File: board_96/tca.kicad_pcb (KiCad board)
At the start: 2 copper layers, 143 x 74 mm, 170 parts, among them IC1 ATMEGA328-A, P1 CONN_2, P2 CONN_3X2, Q1 BSS138, U1 SD_CARD, U10 TLC5941, U11 TLC5941, U12 TLC5941, U13 TLC5941, U14 TLC5941, U15 TLC5941, U2 LD1117S50, U3 LD1117S33, U4 TLC5941, U5 TLC5941, U6 TLC5941, U7 TLC5941, U8 TLC5941, U9 TLC5941, Y1 RESONATEUR

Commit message: Deleted unnecessary files and updated Tlc library.
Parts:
- P1: footprint PIN_ARRAY_2X1 -> PIN_ARRAY_2X1_3960um
- moved C3 3.70 mm to (75.0, 165.7)
- moved P1 2.91 mm to (71.9, 164.7)
- moved 1PIN1 0.50 mm to (207.0, 158.5)
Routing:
- net (no net): track 2096.7 -> 0.00 mm, vias 140 -> 0
- net /tlcs_1-6/VCC: track 80.8 -> 665.3 mm, vias 0 -> 11
- net /tlcs_1-6/SCLK: track 29.4 -> 520.6 mm, vias 12 -> 24
- net /tlcs_1-6/XLAT: track 32.1 -> 521.2 mm, vias 12 -> 19
- net /tlcs_1-6/MODE: track 53.2 -> 528.1 mm, vias 12 -> 29
- net /tlcs_1-6/GSCLK: track 23.5 -> 487.4 mm, vias 12 -> 26
- net /tlcs_1-6/BLANK: track 30.5 -> 405.6 mm, vias 12 -> 20
- net GND: track 400.8 -> 676.8 mm, vias 12 -> 17
- net /tlcs_1-6/SIN: track 2.77 -> 134.9 mm, vias 1 -> 2
- net /MISO: track 0.00 -> 70.2 mm
- net N-00000267: track 4.41 -> 70.7 mm, vias 2 -> 6
- net N-00000183: track 4.41 -> 61.6 mm, vias 2 -> 6
- net N-00000184: track 4.41 -> 60.3 mm, vias 2 -> 6
- net /tlcs_7-12/SIN: track 4.41 -> 56.1 mm, vias 2 -> 1
- net /VSD: track 0.00 -> 47.4 mm, vias 0 -> 2
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- added copper zone on F.Cu, net GND
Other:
- board text added: "TCA96 Rice U Tabor Lab Evan Olson Sebastian Castillo"

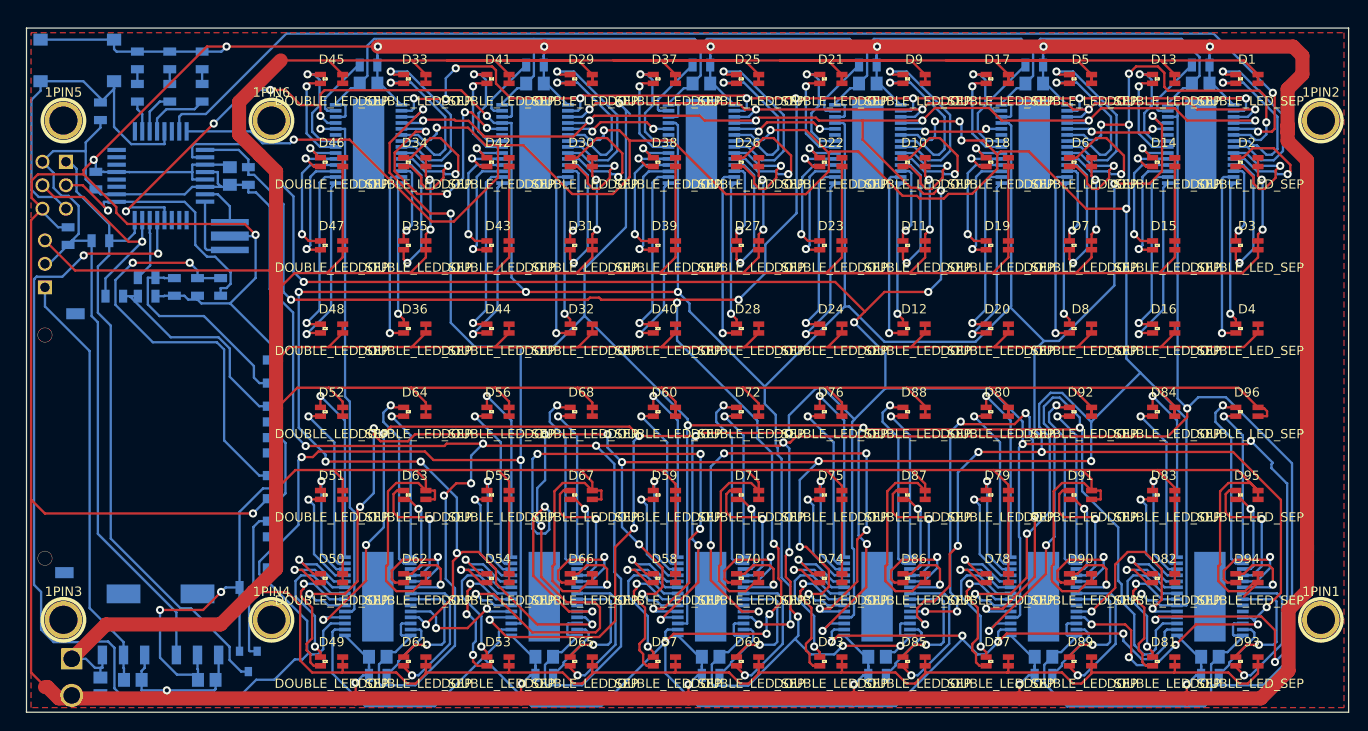
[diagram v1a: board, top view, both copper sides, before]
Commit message: Made board_24_v2 which uses PCB-mounted LED sockets and updated various issues on board_96 as well. These PCBs were ordered around 7/1/14.
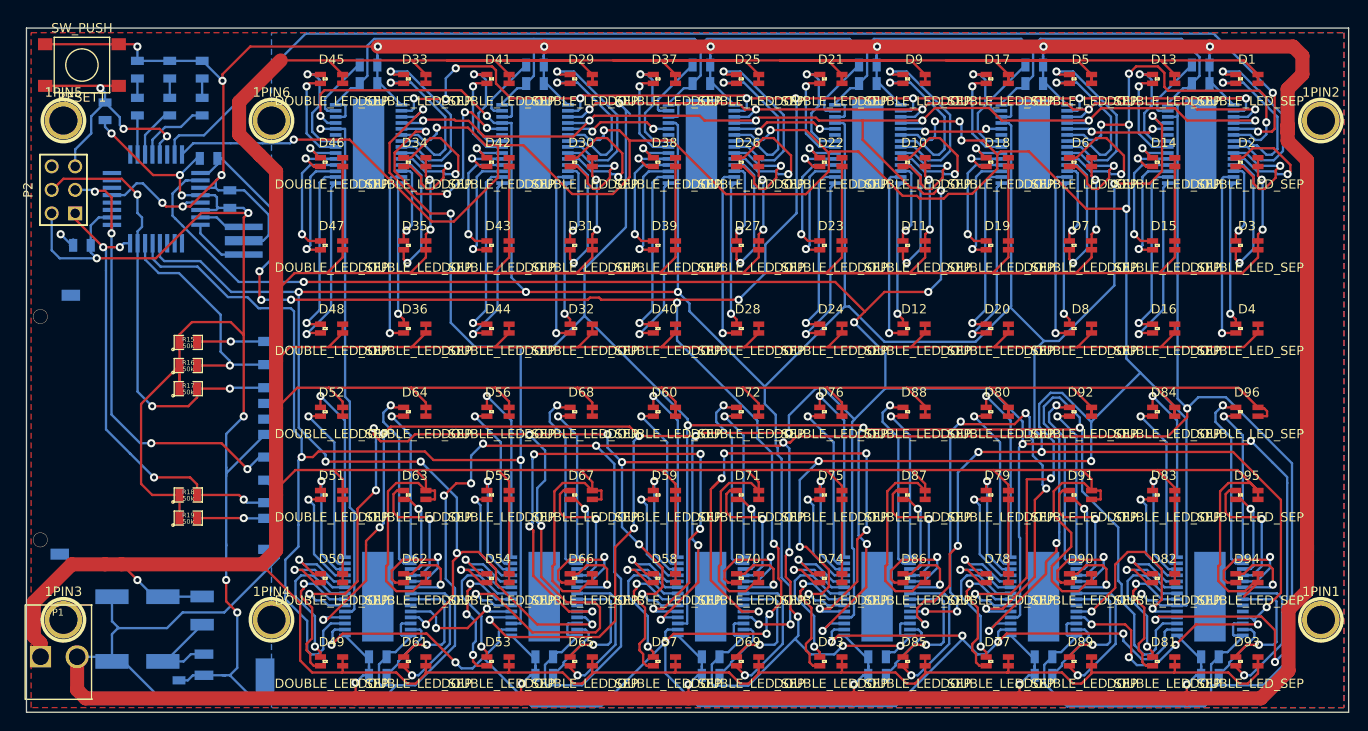
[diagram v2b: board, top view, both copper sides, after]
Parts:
- removed C18: 0.1 uF, c_0805_FIXED
- removed JP1: JUMPER3, PIN_ARRAY_3X1
- removed Q1: BSS138, SOT23
- removed R20, R21, R22: 2.2K, SM0805
- removed U15: TLC5941, TLC5940_FIXED
- added L1: 10uH, SM1210, B.Cu at (86.0, 157.5)
- C1, C10, C11, C12, C13, C14, C15, C16, C17, C2, C5, C7: footprint c_0805_FIXED -> SM0805
- C3, C4: value 100nF -> 47uF; footprint c_0805_FIXED -> c_elec_6.3x5.3
- C6: value 10uF -> 0.1 uF; footprint c_0805_FIXED -> SM0805
- P1, P2, RESET1: moved to F.Cu
- R1: value 10k -> 10K
- R10, R7: value 10K -> 2.2K
- R15, R16, R17, R18, R19: value 2.2K -> 50k; moved to F.Cu
- R2: value 20k -> 10K
- R3, R4, R6, R8: value 10k -> 2.2K
- R5, R9: value 20k -> 2.2K
- U2: value LD1117S50 -> LD1117S33
- U3: value LD1117S33 -> TLC5941; footprint SOT223 -> TLC5940_FIXED
- moved C6 125.4 mm to (194.0, 100.5), turned to 0 degrees
- moved U3 120.3 mm to (194.0, 107.0), turned to 270 degrees
- moved R3 117.5 mm to (194.0, 98.5), turned to 180 degrees
- moved C11 110.1 mm to (104.0, 100.5)
- moved R4 102.6 mm to (176.0, 98.5)
- moved C16 95.8 mm to (177.0, 162.5)
- moved C17 95.8 mm to (195.0, 162.5)
- moved C8 88.1 mm to (158.0, 100.5), turned to 0 degrees
- moved R14 85.9 mm to (195.0, 164.5), turned to 0 degrees
- moved R11 84.6 mm to (141.0, 164.5), turned to 0 degrees
- moved C10 82.9 mm to (122.0, 100.5)
- moved R5 81.9 mm to (158.0, 98.5), turned to 180 degrees
- moved C14 81.6 mm to (141.0, 162.5)
- moved C1 71.8 mm to (89.0, 113.0), turned to 270 degrees
- moved C13 71.2 mm to (123.0, 162.5)
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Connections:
- C4 pad 1: /tlcs_1-6/VCC -> N-0000020
- C5 pad 1: N-0000037 -> /tlcs_1-6/VCC
- C6 pad 1: /VSD -> /tlcs_1-6/VCC
- D1 pad 2: N-00000136 -> N-00000131
- D1 pad 3: N-00000135 -> N-00000130
- D10 pad 2: N-00000120 -> N-00000115
- D10 pad 3: N-00000119 -> N-00000114
- D11 pad 2: N-00000124 -> N-00000119
- D11 pad 3: N-00000122 -> N-00000117
- D12 pad 2: N-00000115 -> N-00000110
- D12 pad 3: N-00000126 -> N-00000121
- D13 pad 2: N-00000143 -> N-00000138
- D13 pad 3: N-00000141 -> N-00000136
- D14 pad 2: N-00000139 -> N-00000134
- D14 pad 3: N-00000150 -> N-00000145
- D15 pad 2: N-00000149 -> N-00000144
- D15 pad 3: N-00000148 -> N-00000143
- D16 pad 2: N-00000147 -> N-00000142
- D16 pad 3: N-00000146 -> N-00000141
- D17 pad 2: N-00000109 -> N-00000104
- D17 pad 3: N-00000107 -> N-00000102
- D18 pad 2: N-00000105 -> N-00000100
- D18 pad 3: N-00000153 -> N-00000148
- D19 pad 2: N-00000152 -> N-00000147
- D19 pad 3: N-00000151 -> N-00000146
- D2 pad 2: N-00000138 -> N-00000133
- D2 pad 3: N-00000137 -> N-00000132
- D20 pad 2: N-00000114 -> N-00000109
- D20 pad 3: N-00000113 -> N-00000108
- D21 pad 2: N-00000125 -> N-00000120
- D21 pad 3: N-00000123 -> N-00000118
- D22 pad 2: N-00000121 -> N-00000116
- D22 pad 3: N-00000133 -> N-00000128
- D23 pad 2: N-00000132 -> N-00000127
- D23 pad 3: N-00000130 -> N-00000125
- D24 pad 2: N-00000129 -> N-00000124
- D24 pad 3: N-00000128 -> N-00000123
- D25 pad 2: N-0000079 -> N-0000073
- D25 pad 3: N-0000080 -> N-0000074
- D26 pad 2: N-0000081 -> N-0000075
- D26 pad 3: N-0000082 -> N-0000076
- D27 pad 2: N-0000083 -> N-0000077
- D27 pad 3: N-0000084 -> N-0000078
- D28 pad 2: N-0000078 -> N-0000072
- D28 pad 3: N-0000077 -> N-0000071
- D29 pad 2: N-0000049 -> N-0000044
- D29 pad 3: N-0000050 -> N-0000045
- D3 pad 2: N-00000142 -> N-00000137
- D3 pad 3: N-00000140 -> N-00000135
- D30 pad 2: N-0000047 -> N-0000042
- D30 pad 3: N-0000048 -> N-0000043
- D31 pad 2: N-0000045 -> N-0000040
- D31 pad 3: N-0000046 -> N-0000041
- D32 pad 2: N-0000043 -> N-0000038
- D32 pad 3: N-0000044 -> N-0000039
- D33 pad 2: N-0000067 (its old number) -> N-0000061
- D33 pad 3: N-0000068 -> N-0000062
- D34 pad 2: N-0000065 (its old number) -> N-0000059
- D34 pad 3: N-0000066 (its old number) -> N-0000060
- D35 pad 2: N-0000064 -> N-0000058
- D35 pad 3: N-0000061 -> N-0000055
- D36 pad 2: N-0000062 -> N-0000056
- D36 pad 3: N-0000063 -> N-0000057
- D37 pad 2: N-0000093 -> N-0000087
- D37 pad 3: N-0000094 -> N-0000088
- D38 pad 2: N-0000095 -> N-0000089
- D38 pad 3: N-0000096 -> N-0000090
- D39 pad 2: N-0000097 -> N-0000091
- D39 pad 3: N-0000060 -> N-0000092
- D4 pad 2: N-00000134 -> N-00000129
- D4 pad 3: N-00000144 -> N-00000139
- D40 pad 2: N-0000098 -> N-0000093
- D40 pad 3: N-0000099 -> N-0000094
- D41 pad 2: N-0000059 -> N-0000054
- D41 pad 3: N-0000058 -> N-0000053
- D42 pad 2: N-0000057 -> N-0000052
- D42 pad 3: N-0000056 -> N-0000051
- D43 pad 2: N-0000055 -> N-0000050
- D43 pad 3: N-0000054 -> N-0000049
- D44 pad 2: N-0000053 -> N-0000048
- D44 pad 3: N-0000052 -> N-0000047
- D45 pad 2: N-0000086 -> N-0000080
- D45 pad 3: N-0000085 -> N-0000079
- D46 pad 2: N-0000087 -> N-0000081
- D46 pad 3: N-0000088 -> N-0000082
- D47 pad 2: N-0000089 -> N-0000083
- D47 pad 3: N-0000090 -> N-0000084
- D48 pad 2: N-0000091 -> N-0000085
- D48 pad 3: N-0000092 -> N-0000086
- D49 pad 2: N-00000248 -> N-00000243
- D49 pad 3: N-00000247 -> N-00000242
- D5 pad 2: N-00000103 -> N-0000098
- D5 pad 3: N-00000102 -> N-0000097
- D50 pad 2: N-00000250 -> N-00000245
- D50 pad 3: N-00000249 -> N-00000244
- D51 pad 2: N-00000254 -> N-00000249
- D51 pad 3: N-00000252 -> N-00000247
- D52 pad 2: N-00000258 -> N-00000253
- D52 pad 3: N-00000256 -> N-00000251
- D53 pad 2: N-00000216 -> N-00000211
- D53 pad 3: N-00000215 -> N-00000210
- D54 pad 2: N-00000213 -> N-00000208
- D54 pad 3: N-00000217 -> N-00000212
- D55 pad 2: N-00000221 -> N-00000216
- D55 pad 3: N-00000219 -> N-00000214
- D56 pad 2: N-00000225 -> N-00000220
- D56 pad 3: N-00000223 -> N-00000218
- D57 pad 2: N-00000229 -> N-00000224
- D57 pad 3: N-00000228 -> N-00000223
- D58 pad 2: N-00000231 -> N-00000226
- D58 pad 3: N-00000230 -> N-00000225
- D59 pad 2: N-00000235 -> N-00000230
- D59 pad 3: N-00000233 -> N-00000228
- D6 pad 2: N-00000104 -> N-0000099
- D6 pad 3: N-00000100 -> N-0000095
- D60 pad 2: N-00000239 -> N-00000234
- D60 pad 3: N-00000237 -> N-00000232
- D61 pad 2: N-00000255 -> N-00000250
- D61 pad 3: N-00000253 -> N-00000248
- D62 pad 2: N-00000251 -> N-00000246
- D62 pad 3: N-00000263 -> N-00000258
- D63 pad 2: N-00000262 (its old number) -> N-00000257
- D63 pad 3: N-00000261 -> N-00000256
- D64 pad 2: N-00000260 -> N-00000255
- D64 pad 3: N-00000259 -> N-00000254
- D65 pad 2: N-00000222 -> N-00000217
- D65 pad 3: N-00000220 -> N-00000215
- D66 pad 2: N-00000218 -> N-00000213
- D66 pad 3: N-00000265 -> N-00000260
- D67 pad 2: N-00000264 -> N-00000259
- D67 pad 3: N-00000240 -> N-00000235
- D68 pad 2: N-00000227 -> N-00000222
- D68 pad 3: N-00000226 -> N-00000221
- D69 pad 2: N-00000236 -> N-00000231
- D69 pad 3: N-00000234 -> N-00000229
- D7 pad 2: N-00000108 -> N-00000103
- D7 pad 3: N-00000106 -> N-00000101
- D70 pad 2: N-00000232 -> N-00000227
- D70 pad 3: N-00000246 -> N-00000241
- D71 pad 2: N-00000245 -> N-00000240
- D71 pad 3: N-00000243 -> N-00000238
- D72 pad 2: N-00000242 -> N-00000237
- D72 pad 3: N-00000241 -> N-00000236
- D73 pad 2: N-00000191 -> N-00000186
- D73 pad 3: N-00000192 -> N-00000187
- D74 pad 2: N-00000193 -> N-00000188
- D74 pad 3: N-00000194 -> N-00000189
- D75 pad 2: N-00000195 -> N-00000190
- D75 pad 3: N-00000196 -> N-00000191
- D76 pad 2: N-00000189 -> N-00000184
- D76 pad 3: N-00000190 -> N-00000185
- D77 pad 2: N-00000162 -> N-00000157
- D77 pad 3: N-00000163 -> N-00000158
- D78 pad 2: N-00000160 -> N-00000155
- D78 pad 3: N-00000161 -> N-00000156
- D79 pad 2: N-00000158 -> N-00000153
- D79 pad 3: N-00000159 -> N-00000154
- D8 pad 2: N-00000112 -> N-00000107
- D8 pad 3: N-00000110 -> N-00000105
- D80 pad 2: N-00000156 -> N-00000151
- D80 pad 3: N-00000157 -> N-00000152
- D81 pad 2: N-00000179 (its old number) -> N-00000174
- D81 pad 3: N-00000180 (its old number) -> N-00000175
- D82 pad 2: N-00000177 -> N-00000172
- D82 pad 3: N-00000178 (its old number) -> N-00000173
- D83 pad 2: N-00000176 -> N-00000171
- D83 pad 3: N-00000173 -> N-00000168
- D84 pad 2: N-00000174 -> N-00000169
- D84 pad 3: N-00000175 -> N-00000170
- D85 pad 2: N-00000206 -> N-00000201
- D85 pad 3: N-00000207 -> N-00000202
- D86 pad 2: N-00000208 -> N-00000203
- D86 pad 3: N-00000205 -> N-00000200
- D87 pad 2: N-00000209 -> N-00000204
- D87 pad 3: N-00000210 -> N-00000205
- D88 pad 2: N-00000211 -> N-00000206
- D88 pad 3: N-00000212 -> N-00000207
- D89 pad 2: N-00000172 -> N-00000167
- D89 pad 3: N-00000171 -> N-00000166
- D9 pad 2: N-00000118 -> N-00000113
- D9 pad 3: N-00000117 -> N-00000112
- D90 pad 2: N-00000170 -> N-00000165
- D90 pad 3: N-00000169 -> N-00000164
- D91 pad 2: N-00000168 -> N-00000163
- D91 pad 3: N-00000167 -> N-00000162
- D92 pad 2: N-00000166 -> N-00000161
- D92 pad 3: N-00000165 -> N-00000160
- D93 pad 2: N-00000197 -> N-00000192
- D93 pad 3: N-00000198 -> N-00000193
- D94 pad 2: N-00000199 -> N-00000194
- D94 pad 3: N-00000200 -> N-00000195
- D95 pad 2: N-00000201 -> N-00000196
- D95 pad 3: N-00000202 -> N-00000197
- D96 pad 2: N-00000203 -> N-00000198
- D96 pad 3: N-00000204 -> N-00000199
- R1 pad 1: /SD_CS -> /RST
- R1 pad 2: /SS -> /tlcs_1-6/VCC
- R10 pad 1: /tlcs_1-6/VCC -> GND
- R10 pad 2: /tlcs_1-6/BLANK -> N-00000261
- R11 pad 2: N-00000155 -> N-00000239
- R12 pad 2: N-00000154 -> N-00000159
- R13 pad 2: N-00000131 -> N-00000183
- R14 pad 2: N-0000051 -> N-00000177
- R15 pad 1: GND -> /tlcs_1-6/VCC
- R15 pad 2: N-0000076 -> N-0000024
- R16 pad 1: GND -> /tlcs_1-6/VCC
- R16 pad 2: N-0000070 -> /SS
- R17 pad 1: GND -> /tlcs_1-6/VCC
- R17 pad 2: N-00000268 -> /MOSI
- R18 pad 1: GND -> /tlcs_1-6/VCC
- R18 pad 2: N-00000266 -> /MISO
- R19 pad 1: GND -> /tlcs_1-6/VCC
- R19 pad 2: N-00000244 -> N-0000019
- R2 pad 1: /SD_CS -> /tlcs_1-6/BLANK
- R2 pad 2: GND -> /tlcs_1-6/VCC
- R3 pad 1: /VSD -> GND
- R3 pad 2: /SD_DataOut -> N-00000150
- R4 pad 1: /SD_DataIn -> GND
- R4 pad 2: /MOSI -> N-00000149
- R5 pad 1: /SD_DataIn -> GND
- R5 pad 2: GND -> N-00000126
- R6 pad 1: /tlcs_1-6/VCC -> GND
- R6 pad 2: /MISO -> N-0000046
- R7 pad 1: /RST -> GND
- R7 pad 2: /tlcs_1-6/VCC -> N-0000070
- R8 pad 1: /SD_SCLK -> GND
- R8 pad 2: /SCK -> N-0000064
- R9 pad 1: /SD_SCLK -> GND
- R9 pad 2: GND -> N-00000263
- U1 pad 1: /SD_CS -> /SS
- U1 pad 2: /SD_DataIn -> /MOSI
- U1 pad 4: /VSD -> /tlcs_1-6/VCC
- U1 pad 5: /SD_SCLK -> /SCK
- U1 pad 7: /SD_DataOut -> /MISO
- U1 pad 8: (no net) -> N-0000019
- U1 pad 9: (no net) -> N-0000024
- U10 pad 10: N-00000250 -> N-00000208
- U10 pad 11: N-00000252 -> N-00000214
- U10 pad 12: N-00000254 -> N-00000216
- U10 pad 13: N-00000256 -> N-00000218
- U10 pad 14: N-00000258 -> N-00000220
- U10 pad 15: N-00000259 -> N-00000221
- U10 pad 16: N-00000260 -> N-00000222
- U10 pad 17: N-00000261 -> N-00000235
- U10 pad 18: N-00000262 (its old number) -> N-00000259
- U10 pad 19: N-00000263 -> N-00000260
- U10 pad 20: N-00000251 -> N-00000213
- U10 pad 21: N-00000253 -> N-00000215
- U10 pad 22: N-00000255 -> N-00000217
- U10 pad 27: N-00000268 -> N-00000261
- U10 pad 5: /tlcs_7-12/SIN -> N-00000209
- U10 pad 7: N-00000247 -> N-00000210
- U10 pad 8: N-00000248 -> N-00000211
- U10 pad 9: N-00000249 -> N-00000212
- U10 pad GND: (no net) -> GND
- U11 pad 10: N-00000213 -> N-00000226
- U11 pad 11: N-00000219 -> N-00000228
- U11 pad 12: N-00000221 -> N-00000230
- U11 pad 13: N-00000223 -> N-00000232
- U11 pad 14: N-00000225 -> N-00000234
- U11 pad 15: N-00000226 -> N-00000236
- U11 pad 16: N-00000227 -> N-00000237
- U11 pad 17: N-00000240 -> N-00000238
- U11 pad 18: N-00000264 -> N-00000240
- U11 pad 19: N-00000265 -> N-00000241
- U11 pad 20: N-00000218 -> N-00000227
- U11 pad 21: N-00000220 -> N-00000229
- U11 pad 22: N-00000222 -> N-00000231
- U11 pad 27: N-00000266 -> N-00000239
- U11 pad 7: N-00000215 -> N-00000223
- U11 pad 8: N-00000216 -> N-00000224
- U11 pad 9: N-00000217 -> N-00000225
- U11 pad GND: (no net) -> GND
- U12 pad 10: N-00000231 -> N-00000188
- U12 pad 11: N-00000233 -> N-00000191
- U12 pad 12: N-00000235 -> N-00000190
- U12 pad 13: N-00000237 -> N-00000185
- U12 pad 14: N-00000239 -> N-00000184
- U12 pad 15: N-00000241 -> N-00000207
- U12 pad 16: N-00000242 -> N-00000206
- U12 pad 17: N-00000243 -> N-00000205
- U12 pad 18: N-00000245 -> N-00000204
- U12 pad 19: N-00000246 -> N-00000200
- U12 pad 20: N-00000232 -> N-00000203
- U12 pad 21: N-00000234 -> N-00000202
- U12 pad 22: N-00000236 -> N-00000201
- U12 pad 27: N-00000244 -> N-00000159
- U12 pad 7: N-00000228 -> N-00000187
- U12 pad 8: N-00000229 -> N-00000186
- U12 pad 9: N-00000230 -> N-00000189
- U12 pad GND: (no net) -> GND
- U13 pad 10: N-00000193 -> N-00000155
- U13 pad 11: N-00000196 -> N-00000154
- U13 pad 12: N-00000195 -> N-00000153
- U13 pad 13: N-00000190 -> N-00000152
- U13 pad 14: N-00000189 -> N-00000151
- U13 pad 15: N-00000212 -> N-00000160
- U13 pad 16: N-00000211 -> N-00000161
- U13 pad 17: N-00000210 -> N-00000162
- U13 pad 18: N-00000209 -> N-00000163
- U13 pad 19: N-00000205 -> N-00000164
- U13 pad 20: N-00000208 -> N-00000165
- U13 pad 21: N-00000207 -> N-00000166
- U13 pad 22: N-00000206 -> N-00000167
- U13 pad 27: N-00000164 -> N-00000183
- U13 pad 7: N-00000192 -> N-00000158
- U13 pad 8: N-00000191 -> N-00000157
- U13 pad 9: N-00000194 -> N-00000156
- U13 pad GND: (no net) -> GND
- U14 pad 10: N-00000160 -> N-00000172
- U14 pad 11: N-00000159 -> N-00000168
- U14 pad 12: N-00000158 -> N-00000171
- U14 pad 13: N-00000157 -> N-00000170
- U14 pad 14: N-00000156 -> N-00000169
- U14 pad 15: N-00000165 -> N-00000199
- U14 pad 16: N-00000166 -> N-00000198
- U14 pad 17: N-00000167 -> N-00000197
- U14 pad 18: N-00000168 -> N-00000196
- U14 pad 19: N-00000169 -> N-00000195
- U14 pad 20: N-00000170 -> N-00000194
- U14 pad 21: N-00000171 -> N-00000193
- U14 pad 22: N-00000172 -> N-00000192
- U14 pad 24: N-00000185 -> (no net)
- U14 pad 27: N-00000188 -> N-00000177
- U14 pad 7: N-00000163 -> N-00000175
- U14 pad 8: N-00000162 -> N-00000174
- U14 pad 9: N-00000161 -> N-00000173
- U14 pad GND: (no net) -> GND
- U2 pad 2: N-0000037 -> /tlcs_1-6/VCC
- U2 pad 3: /tlcs_1-6/VIN -> N-0000020
- U3 pad 2: /VSD -> /tlcs_1-6/BLANK
- U3 pad 3: /tlcs_1-6/VCC -> /tlcs_1-6/XLAT
- U3 pad 4: (no net) -> /tlcs_1-6/SCLK
- U4 pad 10: N-00000138 -> N-0000099
- U4 pad 11: N-00000140 -> N-00000101
- U4 pad 12: N-00000142 -> N-00000103
- U4 pad 13: N-00000144 -> N-00000105
- U4 pad 14: N-00000134 -> N-00000107
- U4 pad 15: N-00000146 -> N-00000108
- U4 pad 16: N-00000147 -> N-00000109
- U4 pad 17: N-00000148 -> N-00000146
- U4 pad 18: N-00000149 -> N-00000147
- U4 pad 19: N-00000150 -> N-00000148
- U4 pad 20: N-00000139 -> N-00000100
- U4 pad 21: N-00000141 -> N-00000102
- U4 pad 22: N-00000143 -> N-00000104
- U4 pad 27: N-00000155 -> N-00000149
- U4 pad 5: /tlcs_1-6/SIN -> N-0000096
- U4 pad 7: N-00000135 -> N-0000097
- U4 pad 8: N-00000136 -> N-0000098
- U4 pad 9: N-00000137 -> N-0000095
- U4 pad GND: (no net) -> GND
- U5 pad 10: N-00000104 -> N-00000115
- U5 pad 11: N-00000106 -> N-00000117
- U5 pad 12: N-00000108 -> N-00000119
- U5 pad 13: N-00000110 -> N-00000121
- U5 pad 14: N-00000112 -> N-00000110
- U5 pad 15: N-00000113 -> N-00000123
- U5 pad 16: N-00000114 -> N-00000124
- U5 pad 17: N-00000151 -> N-00000125
- U5 pad 18: N-00000152 -> N-00000127
- U5 pad 19: N-00000153 -> N-00000128
- U5 pad 20: N-00000105 -> N-00000116
- U5 pad 21: N-00000107 -> N-00000118
- U5 pad 22: N-00000109 -> N-00000120
- U5 pad 27: N-00000154 -> N-00000126
- U5 pad 7: N-00000102 -> N-00000112
- U5 pad 8: N-00000103 -> N-00000113
- U5 pad 9: N-00000100 -> N-00000114
- U5 pad GND: (no net) -> GND
- U6 pad 10: N-00000120 -> N-0000075
- U6 pad 11: N-00000122 -> N-0000078
- U6 pad 12: N-00000124 -> N-0000077
- U6 pad 13: N-00000126 -> N-0000071
- U6 pad 14: N-00000115 -> N-0000072
- U6 pad 15: N-00000128 -> N-0000094
- U6 pad 16: N-00000129 -> N-0000093
- U6 pad 17: N-00000130 -> N-0000092
- U6 pad 18: N-00000132 -> N-0000091
- U6 pad 19: N-00000133 -> N-0000090
- U6 pad 20: N-00000121 -> N-0000089
- U6 pad 21: N-00000123 -> N-0000088
- U6 pad 22: N-00000125 -> N-0000087
- U6 pad 27: N-00000131 -> N-0000046
- U6 pad 7: N-00000117 -> N-0000074
- U6 pad 8: N-00000118 -> N-0000073
- U6 pad 9: N-00000119 -> N-0000076
- U6 pad GND: (no net) -> GND
- U7 pad 10: N-0000081 -> N-0000042
- U7 pad 11: N-0000084 -> N-0000041
- U7 pad 12: N-0000083 -> N-0000040
- U7 pad 13: N-0000077 -> N-0000039
- U7 pad 14: N-0000078 -> N-0000038
- U7 pad 15: N-0000099 -> N-0000047
- U7 pad 16: N-0000098 -> N-0000048
- U7 pad 17: N-0000060 -> N-0000049
- U7 pad 18: N-0000097 -> N-0000050
- U7 pad 19: N-0000096 -> N-0000051
- U7 pad 20: N-0000095 -> N-0000052
- U7 pad 21: N-0000094 -> N-0000053
- U7 pad 22: N-0000093 -> N-0000054
- U7 pad 27: N-0000051 -> N-0000070
- U7 pad 7: N-0000080 -> N-0000045
- U7 pad 8: N-0000079 -> N-0000044
- U7 pad 9: N-0000082 -> N-0000043
- U7 pad GND: (no net) -> GND
- U8 pad 10: N-0000047 -> N-0000059
- U8 pad 11: N-0000046 -> N-0000055
- U8 pad 12: N-0000045 -> N-0000058
- U8 pad 13: N-0000044 -> N-0000057
- U8 pad 14: N-0000043 -> N-0000056
- U8 pad 15: N-0000052 -> N-0000086
- U8 pad 16: N-0000053 -> N-0000085
- U8 pad 17: N-0000054 -> N-0000084
- U8 pad 18: N-0000055 -> N-0000083
- U8 pad 19: N-0000056 -> N-0000082
- U8 pad 20: N-0000057 -> N-0000081
- U8 pad 21: N-0000058 -> N-0000079
- U8 pad 22: N-0000059 -> N-0000080
- U8 pad 24: N-0000073 -> /tlcs_7-12/SIN
- U8 pad 27: N-0000076 -> N-0000064
- U8 pad 7: N-0000050 -> N-0000062
- U8 pad 8: N-0000049 -> N-0000061
- U8 pad 9: N-0000048 -> N-0000060
- U8 pad GND: (no net) -> GND
- U9 pad 10: N-0000065 (its old number) -> N-00000245
- U9 pad 11: N-0000061 -> N-00000247
- U9 pad 12: N-0000064 -> N-00000249
- U9 pad 13: N-0000063 -> N-00000251
- U9 pad 14: N-0000062 -> N-00000253
- U9 pad 15: N-0000092 -> N-00000254
- U9 pad 16: N-0000091 -> N-00000255
- U9 pad 17: N-0000090 -> N-00000256
- U9 pad 18: N-0000089 -> N-00000257
- U9 pad 19: N-0000088 -> N-00000258
- U9 pad 20: N-0000087 -> N-00000246
- U9 pad 21: N-0000085 -> N-00000248
- U9 pad 22: N-0000086 -> N-00000250
- U9 pad 24: /tlcs_7-12/SIN -> N-00000209
- U9 pad 27: N-0000070 -> N-00000263
- U9 pad 5: N-0000073 -> /tlcs_7-12/SIN
- U9 pad 7: N-0000068 -> N-00000242
- U9 pad 8: N-0000067 (its old number) -> N-00000243
- U9 pad 9: N-0000066 (its old number) -> N-00000244
- U9 pad GND: (no net) -> GND
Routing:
- net GND: track 676.8 -> 565.8 mm, vias 17 -> 18
- net /tlcs_1-6/XLAT: track 521.2 -> 461.3 mm, vias 19 -> 17
- net N-00000262: track 13.3 -> 63.5 mm, vias 2 -> 6
- net /VSD: track 47.4 -> 0.00 mm, vias 2 -> 0
- net /SD_SCLK: track 46.1 -> 0.00 mm, vias 2 -> 0
- net N-0000037: track 46.0 -> 0.00 mm
- net N-00000180: track 61.6 -> 21.6 mm, vias 6 -> 2
- net /tlcs_1-6/VCC: track 665.3 -> 697.8 mm, vias 11 -> 18
- net /MOSI: track 23.2 -> 48.0 mm, vias 1 -> 3
- net /SD_DataIn: track 23.5 -> 0.00 mm
- net /SD_CS: track 23.2 -> 0.00 mm
- net /MISO: track 70.2 -> 49.0 mm, vias 0 -> 4
- net N-0000067 (its old number): track 20.2 -> 0.00 mm, vias 1 -> 0
- net N-00000184: track 0.00 -> 19.8 mm, vias 0 -> 1
- net N-0000071: track 0.00 -> 19.5 mm, vias 0 -> 1
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- added copper zone on B.Cu, net GND
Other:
- board text added: "TCA96 v1.1 Rice U Tabor Lab Evan Olson Sebastian Castillo"
- board text removed: "TCA96 Rice U Tabor Lab Evan Olson Sebastian Castillo"
